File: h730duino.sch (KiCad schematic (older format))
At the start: 72 parts, among them J4 105162-0001, J7 Conn_02x03_Odd_Even, P1 CONN_02x18, P10 CONN_01X01, P11 CONN_01X01, P13 CONN_01X01, P2 CONN_01x08, P3 CONN_01x08, P4 CONN_01x08, P5 CONN_01x10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

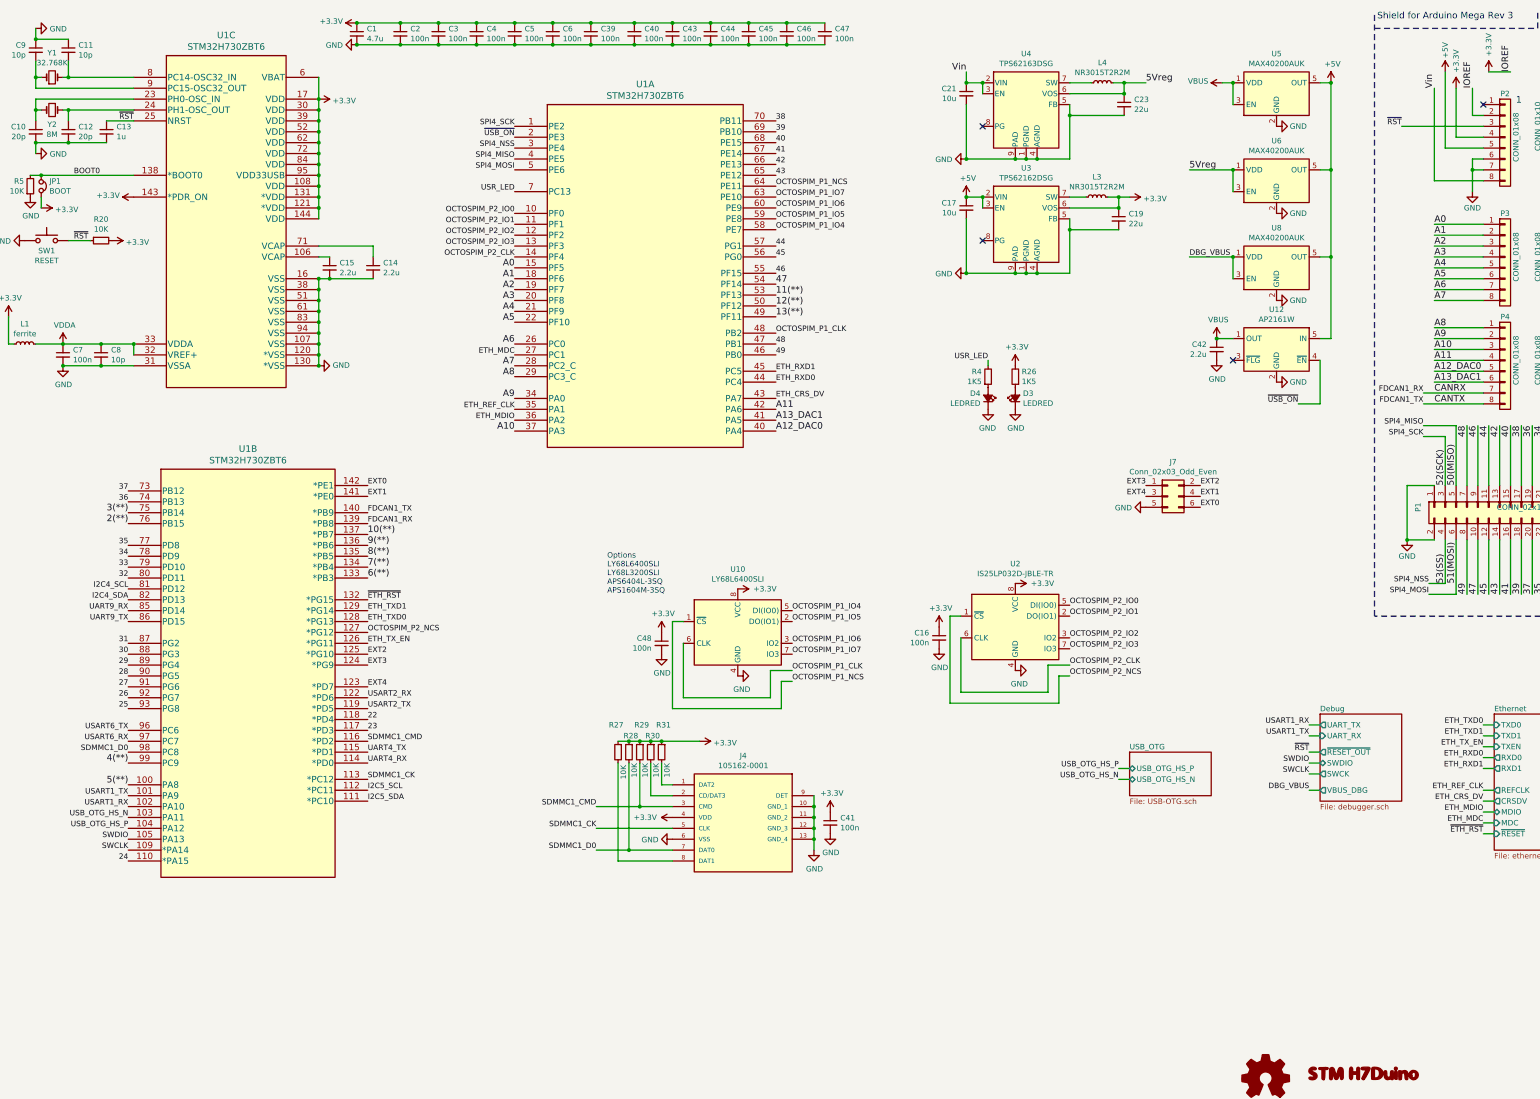
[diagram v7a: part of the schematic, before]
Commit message: Change QSPI PSRAM to hyperRAM
 - Replace QSPI PSRAM to HyperBUS version due to erratasheet
   of mcu (cannot write in QSPI mode without DQS and DQS not
   work in 4bit mode)
 - Connect hyperram to QSPI interface 2
 - Move QSPI flash to interface 1
 - Rearrangue pinouts due to new functionality
 - Remove extra pinouts (now all pins are in arduino connector9
 - Improve schematic and libreries to pass ERC
 - Add pin-1 mark on all IC

Signed-off-by: Martin Ribelotta <martinribelotta@gmail.com>
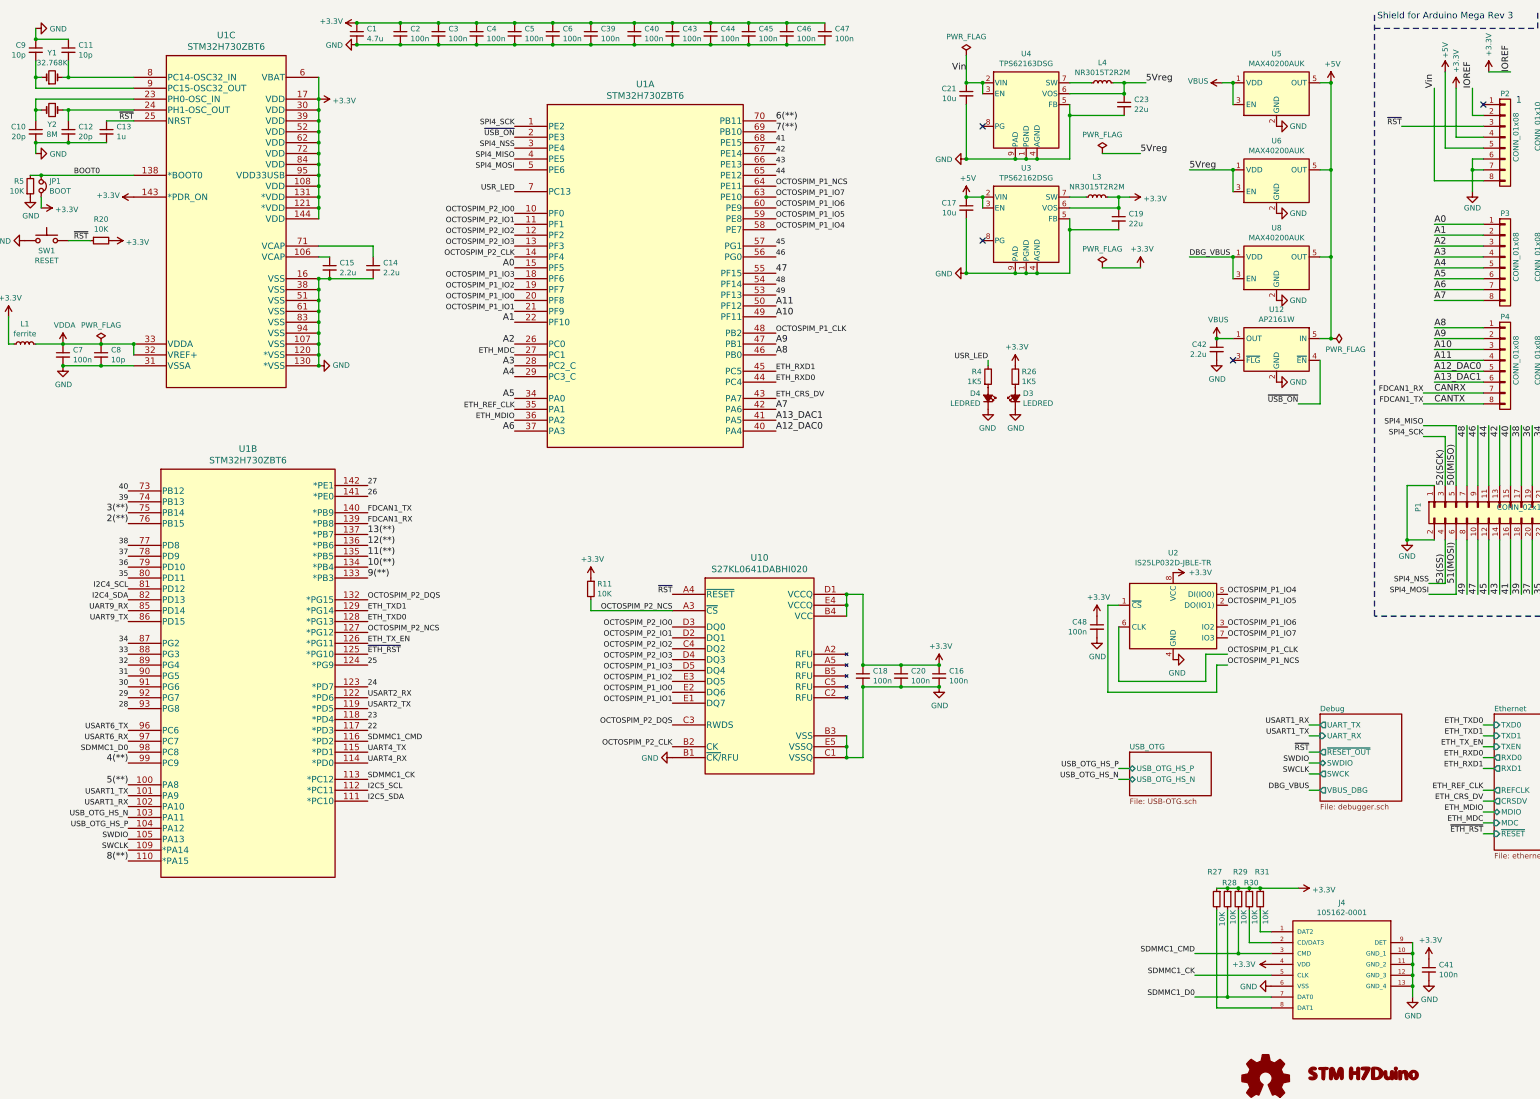
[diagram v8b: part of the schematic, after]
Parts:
- removed J7: Conn_02x03_Odd_Even, Connector_PinHeader_2.54mm:PinHeader_2x03_P2.54mm_Vertical, symbol Connector_Generic:Conn_02x03_Odd_Even
- removed U10: LY68L6400SLI, Package_SO:SOIC-8_3.9x4.9mm_P1.27mm, symbol Memory_Flash:W25Q32JVSS
- added C18, C20: 100n, Capacitor_SMD:C_0603_1608Metric, symbol Device:C_Small
- added R11: 10K, Resistor_SMD:R_0603_1608Metric, symbol Device:R_Small
- added U10: S27KL0641DABHI020, footprints:S27KL0641DABHI020, symbol cyperss-hyperram:S27KL0641DABHI020
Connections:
- net EXT0 is gone; now on net 27: U1.142 (*PE1)
- net EXT1 is gone; now on net 26: U1.141 (*PE0)
- net EXT2 is gone; now on net ~ETH_RST: U1.125 (*PG10)
- net EXT3 is gone; now on net 25: U1.124 (*PG9)
- net EXT4 is gone; now on net 24: U1.123 (*PD7)
- net +3V3: now also C18.1, C20.1, R11.1, U10.B4 (VCC), U10.D1 (VCCQ), U10.E4 (VCCQ)
- net 10(**): now also U1.134 (*PB4); no longer U1.137 (*PB7)
- net 11(**): now also U1.135 (*PB5); no longer U1.53 (PF13)
- net 12(**): now also U1.136 (*PB6); no longer U1.50 (PF12)
- net 13(**): now also U1.137 (*PB7); no longer U1.49 (PF11)
- net 22: now also U1.117 (*PD3); no longer U1.118 (*PD4)
- net 23: now also U1.118 (*PD4); no longer U1.117 (*PD3)
- net 24: no longer U1.110 (*PA15)
- net 25: no longer U1.93 (PG8)
- net 26: no longer U1.92 (PG7)
- net 27: no longer U1.91 (PG6)
- net 28: now also U1.93 (PG8); no longer U1.90 (PG5)
- net 29: now also U1.92 (PG7); no longer U1.89 (PG4)
- net 30: now also U1.91 (PG6); no longer U1.88 (PG3)
- net 31: now also U1.90 (PG5); no longer U1.87 (PG2)
- net 32: now also U1.89 (PG4); no longer U1.80 (PD11)
- net 33: now also U1.88 (PG3); no longer U1.79 (PD10)
- net 34: now also U1.87 (PG2); no longer U1.78 (PD9)
- net 35: now also U1.80 (PD11); no longer U1.77 (PD8)
- net 36: now also U1.79 (PD10); no longer U1.74 (PB13)
- net 37: now also U1.78 (PD9); no longer U1.73 (PB12)
- net 38: now also U1.77 (PD8); no longer U1.70 (PB11)
- net 39: now also U1.74 (PB13); no longer U1.69 (PB10)
- net 40: now also U1.73 (PB12); no longer U1.68 (PE15)
- net 41: now also U1.68 (PE15); no longer U1.67 (PE14)
- net 42: now also U1.67 (PE14); no longer U1.66 (PE13)
- net 43: now also U1.66 (PE13); no longer U1.65 (PE12)
- net 44: now also U1.65 (PE12); no longer U1.57 (PG1)
- net 45: now also U1.57 (PG1); no longer U1.56 (PG0)
- net 46: now also U1.56 (PG0); no longer U1.55 (PF15)
- net 47: now also U1.55 (PF15); no longer U1.54 (PF14)
- net 48: now also U1.54 (PF14); no longer U1.47 (PB1)
- net 49: now also U1.53 (PF13); no longer U1.46 (PB0)
- net 6(**): now also U1.70 (PB11); no longer U1.133 (*PB3)
- net 7(**): now also U1.69 (PB10); no longer U1.134 (*PB4)
- net 8(**): now also U1.110 (*PA15); no longer U1.135 (*PB5)
- net 9(**): now also U1.133 (*PB3); no longer U1.136 (*PB6)
- net A1: now also U1.22 (PF10); no longer U1.18 (PF6)
- net A10: now also U1.49 (PF11); no longer U1.37 (PA3)
- net A11: now also U1.50 (PF12); no longer U1.42 (PA6)
- net A2: now also U1.26 (PC0); no longer U1.19 (PF7)
- net A3: now also U1.28 (PC2_C); no longer U1.20 (PF8)
- net A4: now also U1.29 (PC3_C); no longer U1.21 (PF9)
- net A5: now also U1.34 (PA0); no longer U1.22 (PF10)
- net A6: now also U1.37 (PA3); no longer U1.26 (PC0)
- net A7: now also U1.42 (PA6); no longer U1.28 (PC2_C)
- net A8: now also U1.46 (PB0); no longer U1.29 (PC3_C)
- net A9: now also U1.47 (PB1); no longer U1.34 (PA0)
- net GND: now also C18.2, C20.2, U10.B1 (~CK/~RFU), U10.B3 (VSS), U10.C1 (VSSQ), U10.E5 (VSSQ)
- net OCTOSPIM_P1_CLK: now also U2.6 (CLK)
- net OCTOSPIM_P1_IO4: now also U2.5 (DI(IO0))
- net OCTOSPIM_P1_IO5: now also U2.2 (DO(IO1))
- net OCTOSPIM_P1_IO6: now also U2.3 (IO2)
- net OCTOSPIM_P1_IO7: now also U2.7 (IO3)
- net OCTOSPIM_P1_NCS: now also U2.1 (~CS)
- net OCTOSPIM_P2_CLK: now also U10.B2 (CK); no longer U2.6 (CLK)
- net OCTOSPIM_P2_IO0: now also U10.D3 (DQ0); no longer U2.5 (DI(IO0))
- net OCTOSPIM_P2_IO1: now also U10.D2 (DQ1); no longer U2.2 (DO(IO1))
- net OCTOSPIM_P2_IO2: now also U10.C4 (DQ2); no longer U2.3 (IO2)
- net OCTOSPIM_P2_IO3: now also U10.D4 (DQ3); no longer U2.7 (IO3)
- net OCTOSPIM_P2_NCS: now also R11.2, U10.A3 (~CS); no longer U2.1 (~CS)
- net ~ETH_RST: no longer U1.132 (*PG15)
- net ~RST: now also U10.A4 (~RESET)
- new net OCTOSPIM_P1_IO0: U1.20 (PF8), U10.E2 (DQ6)
- new net OCTOSPIM_P1_IO1: U1.21 (PF9), U10.E1 (DQ7)
- new net OCTOSPIM_P1_IO2: U1.19 (PF7), U10.E3 (DQ5)
- new net OCTOSPIM_P1_IO3: U1.18 (PF6), U10.D5 (DQ4)
- new net OCTOSPIM_P2_DQS: U1.132 (*PG15), U10.C3 (RWDS)
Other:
- note removed: "Options\nLY68L6400SLI\nLY68L3200SLI\nAPS6404L-3SQ\nAPS1604M-3SQ"
- moved on the sheet: C16, C41, C48, J4, R27, R28, R29, R30, R31, U2
